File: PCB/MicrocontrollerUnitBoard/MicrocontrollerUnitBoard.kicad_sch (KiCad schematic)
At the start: 1 part, among them U1 ESP32-S3-WROOM-1

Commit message: 3/1 MCU Board progress upload for board review
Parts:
- added J1, J2: 1769, 1769, symbol Adafruit Accessories JST-PH 2-pin SMT Right Angle Connect:1769
- added J3: 2005280060, CON_2005280060_MOL, symbol WM24188TR-ND:2005280060
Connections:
- net GND: now reaches U1.1 (GND), U1.40 (GND), U1.41 (GND)
- net GND: now also J1.2, J2.2
- net +3.3V: now reaches U1.2 (3V3)
- net +3.3V: now also J1.1, J2.1
- no-connect marks 1 -> 0
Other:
- moved on the sheet: U1

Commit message: recovery attempt
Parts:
- removed U1: ESP32-S3-WROOM-1, RF_Module:ESP32-S3-WROOM-1, symbol RF_Module:ESP32-S3-WROOM-1
- added C1, C2: 0.1uF, symbol Device:C_Small
- added J4: 10118192-0001LF, 10118192-0001LF:AMPHENOL_10118192-0001LF, symbol AMPHENOL_10118192-0001LF:10118192-0001LF
- added R1, R2: 5.1k, symbol Device:R_Small
- added SW1, SW2: PTS526 SM15 SMTR2 LFS, SON4_PTS526 SM15 SMTR2 LFS_CNK, symbol PTS526 SM15 SMTR2 LFS:PTS526_SM15_SMTR2_LFS
- added TP1, TP10, TP11, TP12, TP2, TP3, TP4, TP5, TP6, TP7, TP8, TP9: TestPoint, symbol Connector:TestPoint
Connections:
- net +3.3V: now also R1.1, R2.1, TP10.1
- net GND: now also C1.1, C2.1, J4.5 (GND), SW1.2, SW2.2, TP9.1
- net MOSI: now reaches J3.1
- net MOSI: now also TP8.1
- net MISO: now reaches J3.2
- net MISO: now also TP7.1
- net SCLK: now reaches J3.3
- net SCLK: now also TP6.1
- net CS_N: now reaches J3.4
- net CS_N: now also TP5.1
- net INT_N: now reaches J3.5
- net INT_N: now also TP4.1
- net RST_N: now reaches J3.6
- net RST_N: now also TP3.1
- new net: C1.2, R1.2, SW1.3, TP11.1
- new net: C2.2, R2.2, SW2.3, TP12.1
- new net: J4.3 (D+), TP2.1
- new net: J4.2 (D-), TP1.1

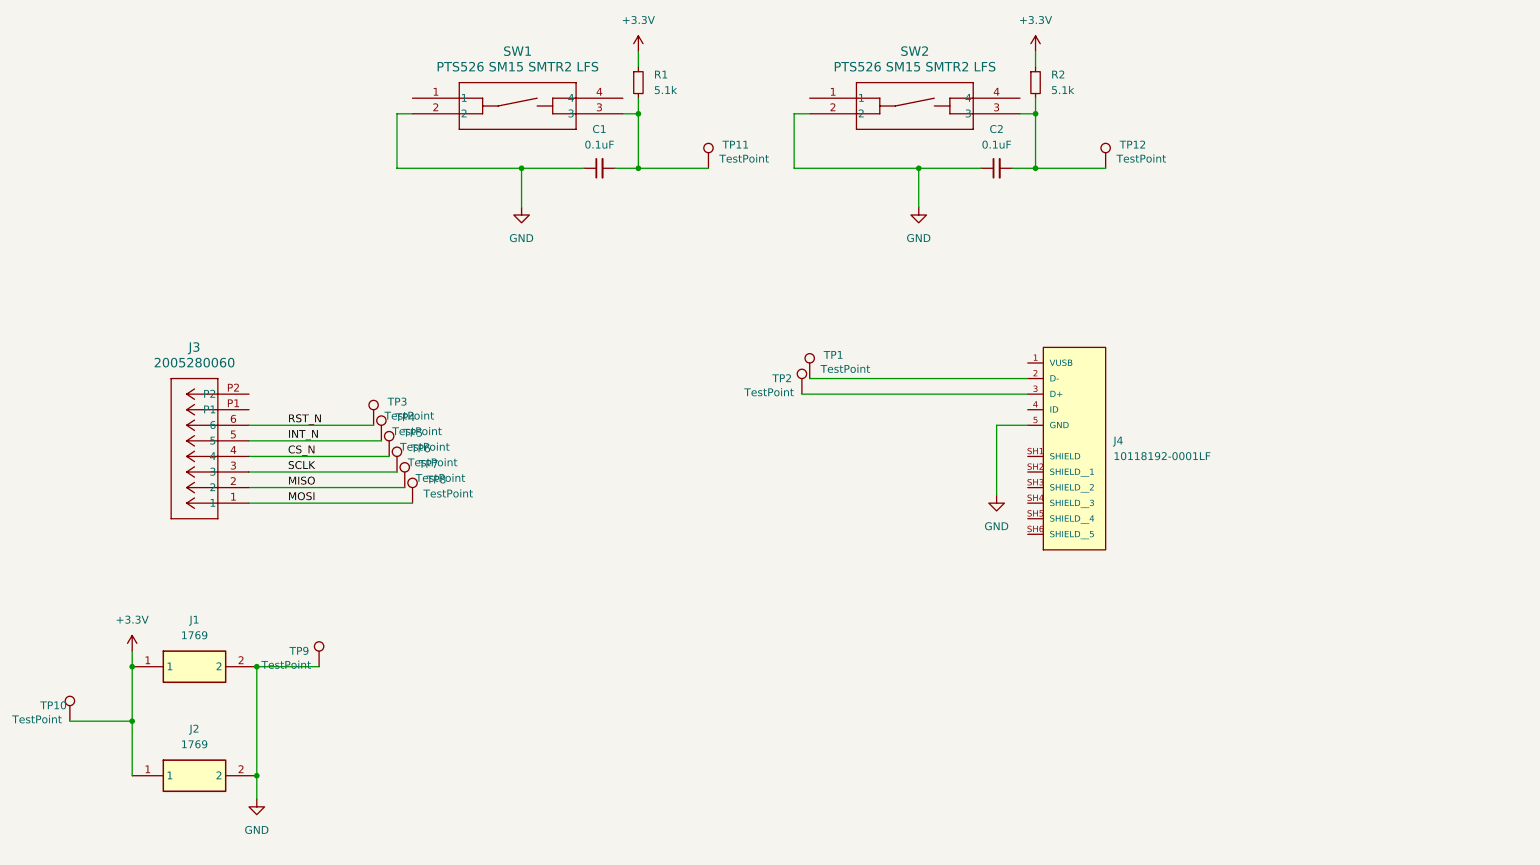
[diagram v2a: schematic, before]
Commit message: Small updates on IMU, initial finish of MCU
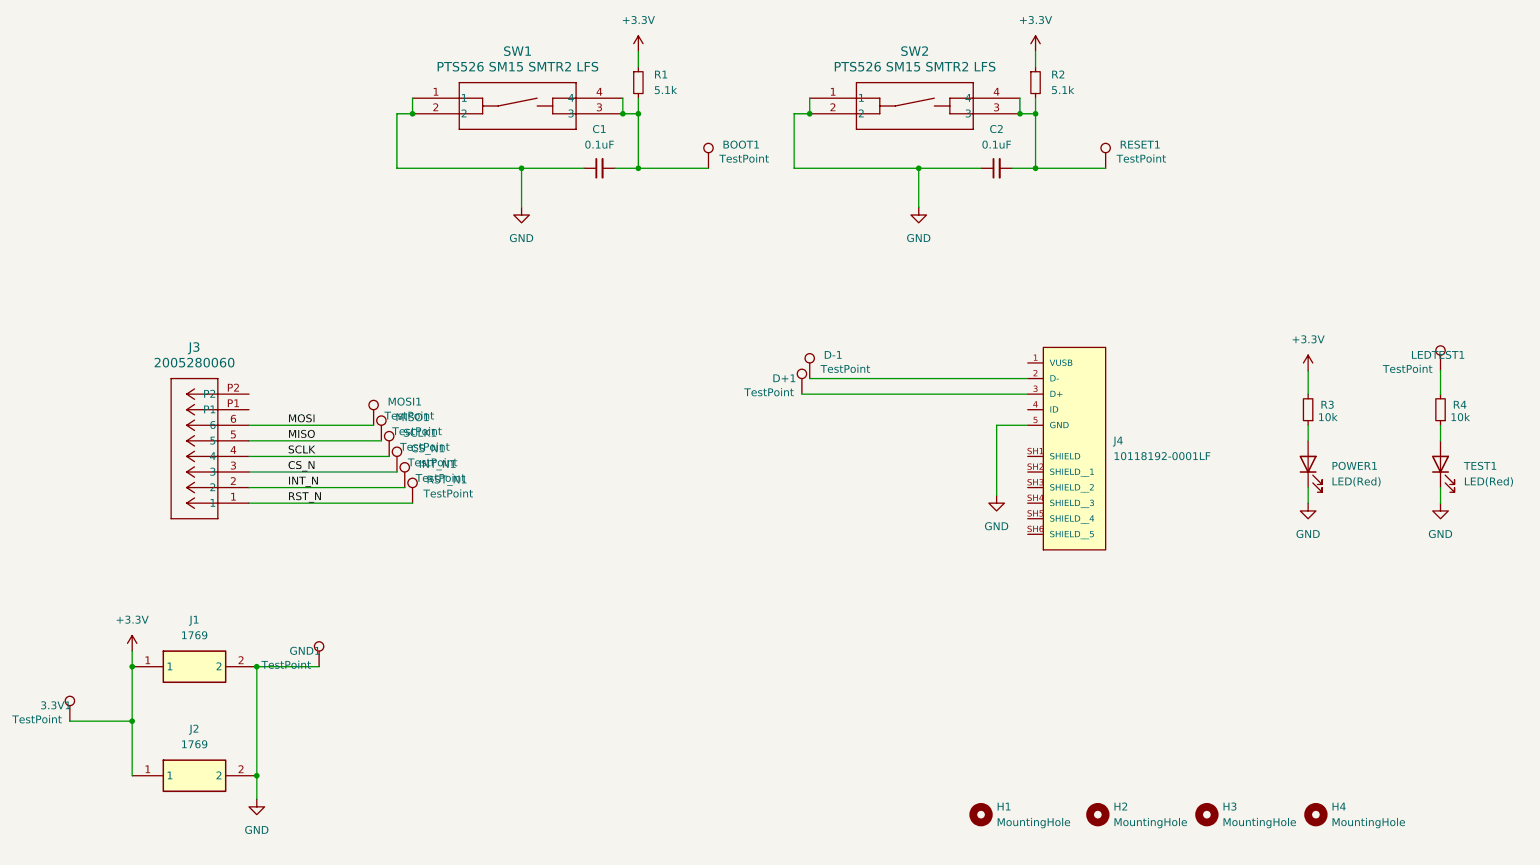
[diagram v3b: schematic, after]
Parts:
- added H1, H2, H3, H4: MountingHole, MountingHole:MountingHole_3.2mm_M3, symbol Mechanical:MountingHole
- added LEDTEST1: TestPoint, TestPoint:TestPoint_THTPad_D2.0mm_Drill1.0mm, symbol Connector:TestPoint
- added POWER1, TEST1: LED(Red), LED_SMD:LED_0603_1608Metric_Pad1.05x0.95mm_HandSolder, symbol Device:LED
- added R3, R4: 10k, Resistor_SMD:R_0805_2012Metric_Pad1.20x1.40mm_HandSolder, symbol Device:R_Small
- 3.3V1: renamed from TP10; footprint (none) -> TestPoint:TestPoint_THTPad_D2.0mm_Drill1.0mm
- BOOT1: renamed from TP11; footprint (none) -> TestPoint:TestPoint_THTPad_D2.0mm_Drill1.0mm
- C1, C2: footprint (none) -> Capacitor_SMD:C_0805_2012Metric_Pad1.18x1.45mm_HandSolder
- CS_N1: renamed from TP6; footprint (none) -> TestPoint:TestPoint_THTPad_D2.0mm_Drill1.0mm
- D+1: renamed from TP2; footprint (none) -> TestPoint:TestPoint_THTPad_D2.0mm_Drill1.0mm
- D-1: renamed from TP1; footprint (none) -> TestPoint:TestPoint_THTPad_D2.0mm_Drill1.0mm
- GND1: renamed from TP9; footprint (none) -> TestPoint:TestPoint_THTPad_D2.0mm_Drill1.0mm
- INT_N1: renamed from TP7; footprint (none) -> TestPoint:TestPoint_THTPad_D2.0mm_Drill1.0mm
- J1, J2: footprint 1769 -> Adafruit Accessories JST-PH 2-pin SMT Right Angle Connect:1769
- J3: footprint CON_2005280060_MOL -> WM24188TR-ND:CON_2005280060_MOL
- J4: footprint 10118192-0001LF:AMPHENOL_10118192-0001LF -> AMPHENOL_10118192-0001LF:AMPHENOL_10118192-0001LF
- MISO1: renamed from TP4; footprint (none) -> TestPoint:TestPoint_THTPad_D2.0mm_Drill1.0mm
- MOSI1: renamed from TP3; footprint (none) -> TestPoint:TestPoint_THTPad_D2.0mm_Drill1.0mm
- R1, R2: footprint (none) -> Resistor_SMD:R_0805_2012Metric_Pad1.20x1.40mm_HandSolder
- RESET1: renamed from TP12; footprint (none) -> TestPoint:TestPoint_THTPad_D2.0mm_Drill1.0mm
- RST_N1: renamed from TP8; footprint (none) -> TestPoint:TestPoint_THTPad_D2.0mm_Drill1.0mm
- SCLK1: renamed from TP5; footprint (none) -> TestPoint:TestPoint_THTPad_D2.0mm_Drill1.0mm
- SW1, SW2: footprint SON4_PTS526 SM15 SMTR2 LFS_CNK -> PTS526 SM15 SMTR2 LFS:SON4_PTS526 SM15 SMTR2 LFS_CNK
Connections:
- net +3.3V: now also R3.2
- net CS_N: now also CS_N1.1, J3.3; no longer J3.4, SCLK1.1
- net GND: now also SW1.1, SW2.1, POWER1.1 (K), TEST1.1 (K)
- net INT_N: now also INT_N1.1, J3.2; no longer J3.5, MISO1.1
- net MISO: now also J3.5, MISO1.1; no longer INT_N1.1, J3.2
- net MOSI: now also J3.6, MOSI1.1; no longer J3.1, RST_N1.1
- net RST_N: now also J3.1, RST_N1.1; no longer J3.6, MOSI1.1
- net SCLK: now also J3.4, SCLK1.1; no longer CS_N1.1, J3.3
- net at BOOT1.1, C1.2, R1.2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: now also SW1.4
- net at C2.2, R2.2, RESET1.1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: now also SW2.4
- new net: R4.1, TEST1.2 (A)
- new net: POWER1.2 (A), R3.1
- new net: LEDTEST1.1, R4.2

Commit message: Finish MCU Test board
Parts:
- added 3.3V2, 3.3V3, 3.3V4, GND2, GND3, GND4, GND5: TestPoint, TestPoint:TestPoint_THTPad_D2.0mm_Drill1.0mm, symbol Connector:TestPoint
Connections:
- net +3.3V: now also 3.3V2.1, 3.3V3.1, 3.3V4.1
- net GND: now also GND2.1, GND3.1, GND4.1, GND5.1
